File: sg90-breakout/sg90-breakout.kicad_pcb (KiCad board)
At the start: 2 copper layers, 17.3 x 9.4 mm, 3 parts, among them J1 Conn_01x03, J2 Conn_01x05_MountingPin, M1 Motor_DC

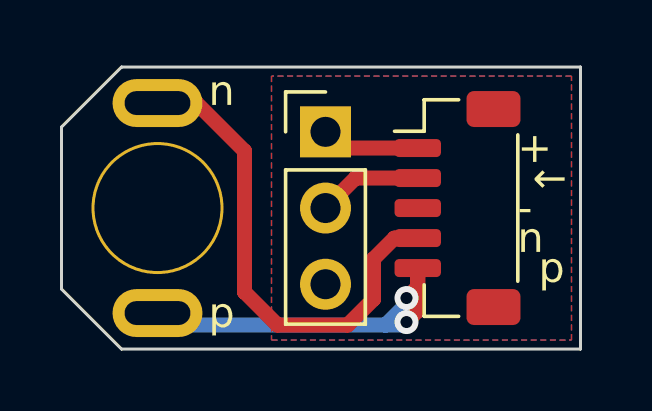
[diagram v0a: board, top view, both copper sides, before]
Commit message: vertical and horizontal connector footprints
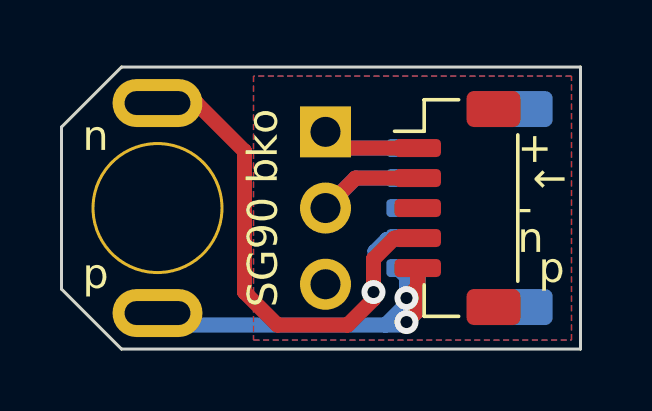
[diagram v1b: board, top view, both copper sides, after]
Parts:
- added J3: Conn_01x05_MountingPin, Connector_JST:JST_SH_SM05B-SRSS-TB_1x05-1MP_P1.00mm_Horizontal, B.Cu at (113.6, 95.3)
- J1: value Conn_01x03 -> pot
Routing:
- net /motp: track 13.6 -> 18.7 mm
- net /motn: track 16.5 -> 20.0 mm, vias 0 -> 1
- net Net-(J1-Pin_2): track 3.49 -> 6.60 mm
- net Net-(J1-Pin_1): track 3.30 -> 6.22 mm
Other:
- board text added: "SG90 bko"
- board text added: "Valpo ECE"
- board text removed: "SG90 breakout"
- board text removed: "Valpo ECE DJW"

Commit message: tweak silkscreen
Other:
- board text added: "DJW 2024"
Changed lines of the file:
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@@
     (property "ki_description" "Generic connectable mounting pin connector, single row, 01x05, script generated (kicad-library-utils/schlib/autogen/connector/)")
     (property "ki_keywords" "connector")
-    (attr smd exclude_from_pos_files exclude_from_bom)
+    (attr smd)
     (fp_text reference "J2" (at 0 -3.3 90) (layer "F.SilkS") hide
         (effects (font (size 1 1) (thickness 0.15)))
@@
     (pad "5" smd roundrect (at 2 2 270) (size 0.6 1.55) (layers "B.Cu" "B.Paste" "B.Mask") (roundrect_rratio 0.25)
       (net 5 "/motp") (pinfunction "Pin_5") (pintype "passive"))
-    (pad "MP" smd roundrect (at -3.3 -1.875 270) (size 1.2 1.8) (layers "B.Cu" "B.Paste" "B.Mask") (roundrect_rratio 0.208333)
+    (pad "MP" smd roundrect (at -3.3 -1.875 270) (size 1.2 1.8) (layers "B.Cu" "B.Paste" "B.Mask") (roundrect_rratio 0.2083333333)
       (net 3 "GND") (pinfunction "MountPin") (pintype "passive"))
-    (pad "MP" smd roundrect (at 3.3 -1.875 270) (size 1.2 1.8) (layers "B.Cu" "B.Paste" "B.Mask") (roundrect_rratio 0.208333)
+    (pad "MP" smd roundrect (at 3.3 -1.875 270) (size 1.2 1.8) (layers "B.Cu" "B.Paste" "B.Mask") (roundrect_rratio 0.2083333333)
       (net 3 "GND") (pinfunction "MountPin") (pintype "passive"))
     (model "${KICAD7_3DMODEL_DIR}/Connector_JST.3dshapes/JST_SH_SM05B-SRSS-TB_1x05-1MP_P1.00mm_Horizontal.wrl"
@@
     )
     (stroke (width 0.1) (type solid)) (fill none) (layer "Edge.Cuts"))
+  (gr_text "DJW 2024" (at 113.6 95.3 90) (layer "B.SilkS")
+    (effects (font (size 1 1) (thickness 0.15)) (justify mirror))
+  )
   (gr_text "Valpo ECE" (at 106.2 95.3 90) (layer "B.SilkS")
     (effects (font (size 1 1) (thickness 0.15)) (justify mirror))

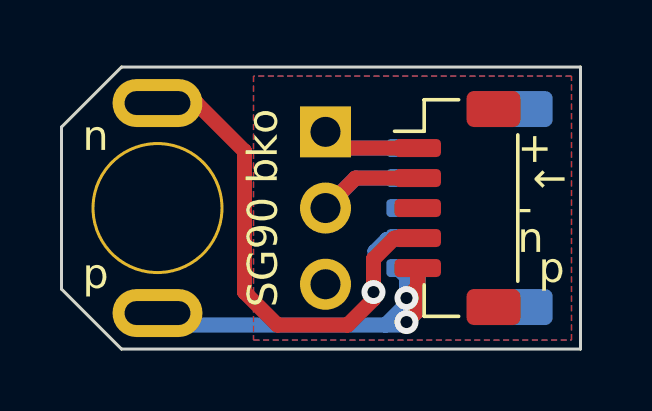
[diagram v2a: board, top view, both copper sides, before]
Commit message: Renumber pins to match rotations
Viewed from top:
* counter-clockwise is increasing pulse-width for normal servo
* positive P-N to motor gives CCW output rotation
* CCW rotation moves pot wiper towards "top" of pot
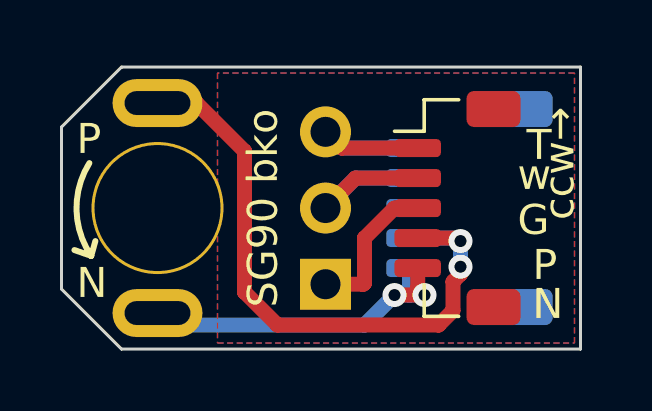
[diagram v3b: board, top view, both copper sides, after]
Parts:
- moved J1 5.08 mm to (108.8, 97.8), turned to 180 degrees
- turned M1 to 180 degrees
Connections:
- J1 pad 1: Net-(J1-Pin_1) -> /GND
- J1 pad 3: GND -> Net-(J1-Pin_3)
- J2 pad 1: Net-(J1-Pin_1) -> Net-(J1-Pin_3)
- J2 pad 3: GND -> /GND
- J2 pad 4: /motn -> /motp
- J2 pad 5: /motp -> /motn
- J2 pad MP: GND -> /GND
- J3 pad 1: Net-(J1-Pin_1) -> Net-(J1-Pin_3)
- J3 pad 3: GND -> /GND
- J3 pad 4: /motn -> /motp
- J3 pad 5: /motp -> /motn
- J3 pad MP: GND -> /GND
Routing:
- net /motn: track 20.0 -> 12.4 mm, vias 1 -> 2
- net Net-(J1-Pin_3): track 0.00 -> 6.22 mm
- net Net-(J1-Pin_1): track 6.22 -> 0.00 mm
- net /GND: track 0.00 -> 5.01 mm
- net /motp: track 18.7 -> 21.6 mm
- added copper zone on B.Cu, net /GND
- added copper zone on F.Cu, net /GND
- removed copper zone on B.Cu, net GND
- removed copper zone on F.Cu, net GND
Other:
- board text added: "2024"
- board text added: "DJW"
- board text added: "G"
- board text added: "N"
- board text added: "P"
- board text added: "T"
- board text added: "ccw→"
- board text added: "w"
- board text removed: "+"
- board text removed: "-"
- board text removed: "DJW 2024"
- board text removed: "n"
- board text removed: "p"
- board text removed: "←"

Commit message: Add JLC tag for production
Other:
- board text added: "JLCJLCJLCJLC"
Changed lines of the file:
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@@
     )
     (stroke (width 0.1) (type solid)) (fill none) (layer "Edge.Cuts"))
+  (gr_text "JLCJLCJLCJLC" (at 114.7 99.9) (layer "B.SilkS")
+    (effects (font (size 1 0.85) (thickness 0.15) bold) (justify left bottom mirror))
+  )
   (gr_text "DJW" (at 113.5 93.8 90) (layer "B.SilkS")
     (effects (font (size 1 1) (thickness 0.15)) (justify mirror))
   )
-  (gr_text "Valpo ECE" (at 106.5 95.3 90) (layer "B.SilkS")
+  (gr_text "Valpo ECE" (at 106.5 94.8 90) (layer "B.SilkS")
     (effects (font (size 1 1) (thickness 0.15)) (justify mirror))
   )

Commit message: remove JLC order number tag
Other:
- board text removed: "JLCJLCJLCJLC"
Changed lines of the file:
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@@
     )
     (stroke (width 0.1) (type solid)) (fill none) (layer "Edge.Cuts"))
-  (gr_text "JLCJLCJLCJLC" (at 114.7 99.9) (layer "B.SilkS")
-    (effects (font (size 1 0.85) (thickness 0.15) bold) (justify left bottom mirror))
-  )
   (gr_text "DJW" (at 113.5 93.8 90) (layer "B.SilkS")
     (effects (font (size 1 1) (thickness 0.15)) (justify mirror))
